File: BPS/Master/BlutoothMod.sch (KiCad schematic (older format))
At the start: 12 parts, among them SW2 SW_DIP_x01, U6 RN4870-V_RM118, U7 MCP100-315D

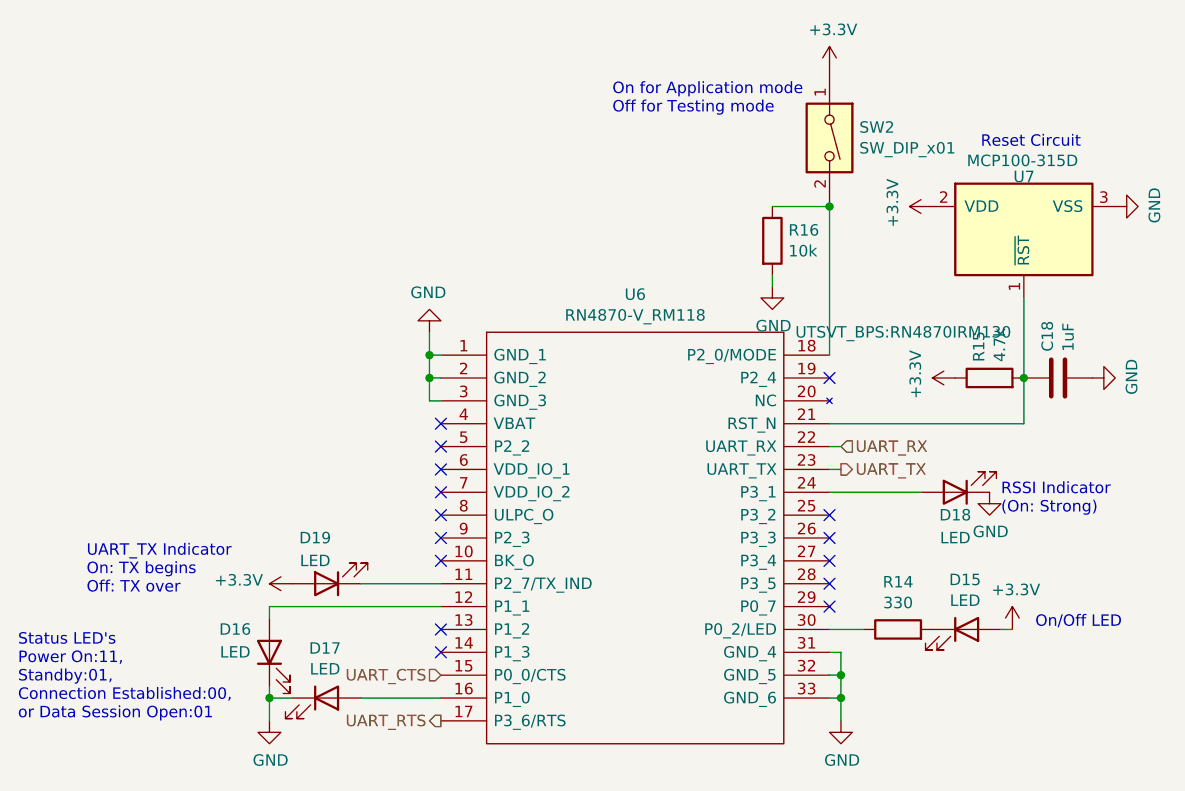
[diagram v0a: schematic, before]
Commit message: Assigned footprints to all symbols except reset circuit(high voltage detector). Changed 18 pin connector to 3, 6 pin connectors. Generated netlist.
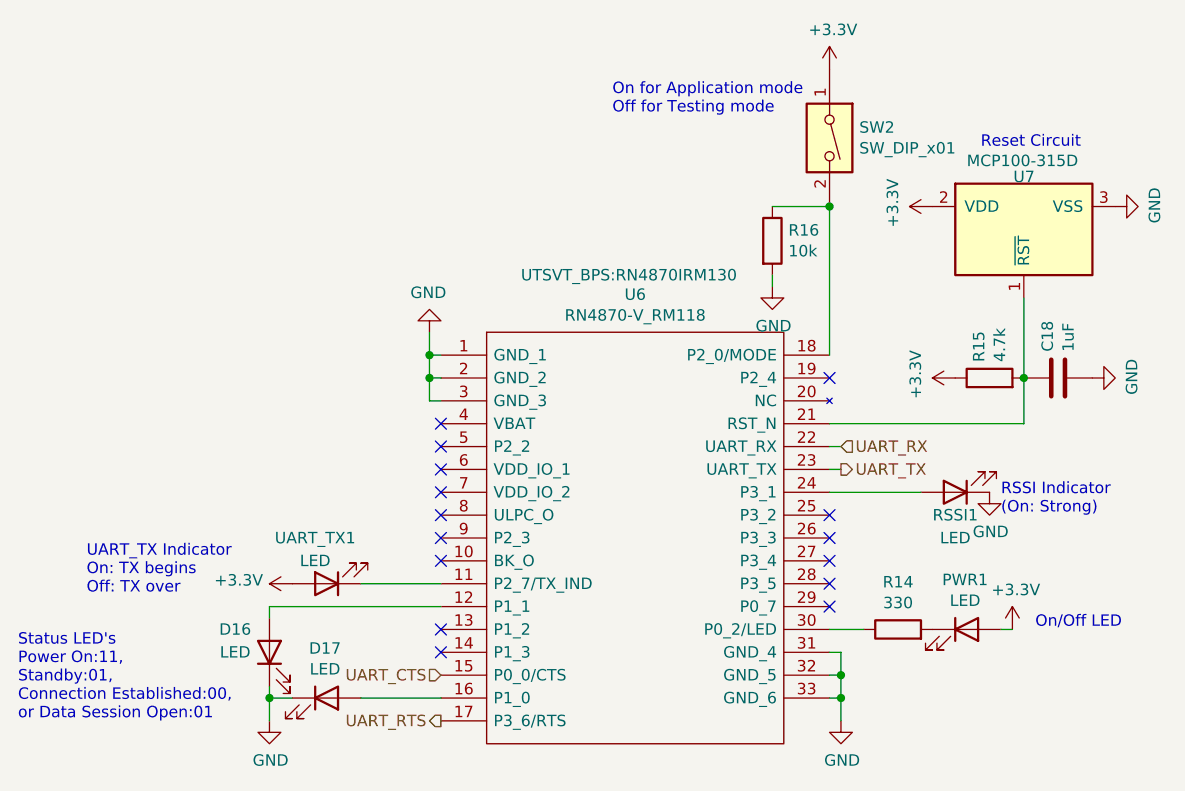
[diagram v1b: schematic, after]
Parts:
- C18: footprint (none) -> Capacitor_SMD:C_0805_2012Metric
- D16, D17: footprint (none) -> LED_SMD:LED_0805_2012Metric
- PWR1: renamed from D15; footprint (none) -> LED_SMD:LED_0805_2012Metric
- R14, R15, R16: footprint (none) -> Resistor_SMD:R_0805_2012Metric
- RSSI1: renamed from D18; footprint (none) -> LED_SMD:LED_0805_2012Metric
- SW2: footprint (none) -> Button_Switch_SMD:SW_DIP_SPSTx01_Slide_6.7x4.1mm_W6.73mm_P2.54mm_LowProfile_JPin
- UART_TX1: renamed from D19; footprint (none) -> LED_SMD:LED_0805_2012Metric
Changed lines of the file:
@@
 F 0 "U6" H 5850 3165 50  0000 C CNN
 F 1 "RN4870-V_RM118" H 5850 3074 50  0000 C CNN
-F 2 "UTSVT_BPS:RN4870IRM130" H 6550 3000 50  0000 L CNN
+F 2 "UTSVT_BPS:RN4870IRM130" H 5350 3250 50  0000 L CNN
 F 3 "http://docs-emea.rs-online.com/webdocs/152f/0900766b8152ff8f.pdf" H 6550 2900 50  0001 L CNN
 F 4 "Microchip RN4870-V/RM118 Bluetooth Chip 4.2" H 6550 2800 50  0001 L CNN "Description"
@@
 F 0 "R15" H 7470 3046 50  0000 L CNN
 F 1 "4.7k" H 7470 2955 50  0000 L CNN
-F 2 "" V 7330 3000 50  0001 C CNN
+F 2 "Resistor_SMD:R_0805_2012Metric" V 7330 3000 50  0001 C CNN
 F 3 "~" H 7400 3000 50  0001 C CNN
 	1    7400 3000
@@
 F 0 "C18" H 7815 3046 50  0000 L CNN
 F 1 "1uF" H 7815 2955 50  0000 L CNN
-F 2 "" H 7738 2850 50  0001 C CNN
+F 2 "Capacitor_SMD:C_0805_2012Metric" H 7738 2850 50  0001 C CNN
 F 3 "~" H 7700 3000 50  0001 C CNN
 	1    7700 3000
@@
 F 0 "R14" V 7207 4100 50  0000 C CNN
 F 1 "330" V 7116 4100 50  0000 C CNN
-F 2 "" V 6930 4100 50  0001 C CNN
+F 2 "Resistor_SMD:R_0805_2012Metric" V 6930 4100 50  0001 C CNN
 F 3 "~" H 7000 4100 50  0001 C CNN
 	1    7000 4100
@@
 	6700 4100 6850 4100
 $Comp
-L Device:LED D15
+L Device:LED PWR1
 U 1 1 5EE14D8D
 P 7300 4100
-F 0 "D15" H 7293 4317 50  0000 C CNN
+F 0 "PWR1" H 7293 4317 50  0000 C CNN
 F 1 "LED" H 7293 4226 50  0000 C CNN
-F 2 "" H 7300 4100 50  0001 C CNN
+F 2 "LED_SMD:LED_0805_2012Metric" H 7300 4100 50  0001 C CNN
 F 3 "~" H 7300 4100 50  0001 C CNN
 	1    7300 4100
@@
 F 0 "D16" V 4350 4350 50  0000 C CNN
 F 1 "LED" V 4250 4350 50  0000 C CNN
-F 2 "" H 4250 4200 50  0001 C CNN
+F 2 "LED_SMD:LED_0805_2012Metric" H 4250 4200 50  0001 C CNN
 F 3 "~" H 4250 4200 50  0001 C CNN
 	1    4250 4200
@@
 F 0 "D17" H 4493 4617 50  0000 C CNN
 F 1 "LED" H 4493 4526 50  0000 C CNN
-F 2 "" H 4500 4400 50  0001 C CNN
+F 2 "LED_SMD:LED_0805_2012Metric" H 4500 4400 50  0001 C CNN
 F 3 "~" H 4500 4400 50  0001 C CNN
 	1    4500 4400
@@
 	7550 3200 7550 3000
 $Comp
-L Device:LED D18
+L Device:LED RSSI1
 U 1 1 5EE54DD1
 P 7250 3500
-F 0 "D18" H 7250 3600 50  0000 C CNN
+F 0 "RSSI1" H 7250 3600 50  0000 C CNN
 F 1 "LED" H 7250 3700 50  0000 C CNN
-F 2 "" H 7250 3500 50  0001 C CNN
+F 2 "LED_SMD:LED_0805_2012Metric" H 7250 3500 50  0001 C CNN
 F 3 "~" H 7250 3500 50  0001 C CNN
 	1    7250 3500
@@
 RSSI Indicator\n(On: Strong)
 $Comp
-L Device:LED D19
+L Device:LED UART_TX1
 U 1 1 5EE52339
 P 4500 3900
-F 0 "D19" H 4550 3700 50  0000 C CNN
+F 0 "UART_TX1" H 4550 3700 50  0000 C CNN
 F 1 "LED" H 4550 3800 50  0000 C CNN
-F 2 "" H 4500 3900 50  0001 C CNN
+F 2 "LED_SMD:LED_0805_2012Metric" H 4500 3900 50  0001 C CNN
 F 3 "~" H 4500 3900 50  0001 C CNN
 	1    4500 3900
@@
 F 0 "SW2" V 6654 2080 50  0000 L CNN
 F 1 "SW_DIP_x01" V 6745 2080 50  0000 L CNN
-F 2 "" H 6700 1950 50  0001 C CNN
+F 2 "Button_Switch_SMD:SW_DIP_SPSTx01_Slide_6.7x4.1mm_W6.73mm_P2.54mm_LowProfile_JPin" H 6700 1950 50  0001 C CNN
 F 3 "~" H 6700 1950 50  0001 C CNN
 	1    6700 1950
@@
 F 0 "R16" H 6520 2446 50  0000 L CNN
 F 1 "10k" H 6520 2355 50  0000 L CNN
-F 2 "" V 6380 2400 50  0001 C CNN
+F 2 "Resistor_SMD:R_0805_2012Metric" V 6380 2400 50  0001 C CNN
 F 3 "~" H 6450 2400 50  0001 C CNN
 	1    6450 2400

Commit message: Made file paths of symbol libraries relative. Added footprint for high voltage detection that is SMD and has same specs as one recommended in Bluetooth Module datasheet.
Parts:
- U7: footprint (none) -> UTSVT_BPS:SOT96P240X110-3N
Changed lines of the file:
@@
 F 0 "U7" V 7320 2396 50  0000 R CNN
 F 1 "MCP100-315D" V 7250 2600 50  0000 R CNN
-F 2 "" H 7150 2500 50  0001 C CNN
+F 2 "UTSVT_BPS:SOT96P240X110-3N" H 7150 2500 50  0001 C CNN
 F 3 "http://ww1.microchip.com/downloads/en/DeviceDoc/11187f.pdf" H 7250 2600 50  0001 C CNN
 	1    7550 2350
